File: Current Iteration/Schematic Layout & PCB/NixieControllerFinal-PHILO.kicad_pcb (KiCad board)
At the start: 2 copper layers, 47.3 x 96.8 mm, 100 parts, among them J1 Conn_01x10_Pin, J10 Conn_ARM_SWD_TagConnect_TC2030, J11 Conn_01x04_Socket, J12 Conn_01x03_Socket, J13 Conn_01x03_Socket, J16 Conn_01x08_Socket, J2 JST_EH_B4B, J3 Conn_01x10_Pin, J4 Conn_01x10_Pin, J5 Conn_01x10_Pin, J6 Conn_01x02, J7 Micro_SD_Card_Det1, J9 NixieIN, U1 HV5622PG, U10 NID1100, U11 TPS61040DBV, U13 STM32G0B1KEU6, U14 CM1224-04MR, U2 HV5622PG, U3 4504, U4 CM1224-04MR, U5 NCH6100HV, U6 CAP1206-x-SL, U7 NID1100, U8 MCP1700x-330xxTT, U9 MAX98357A

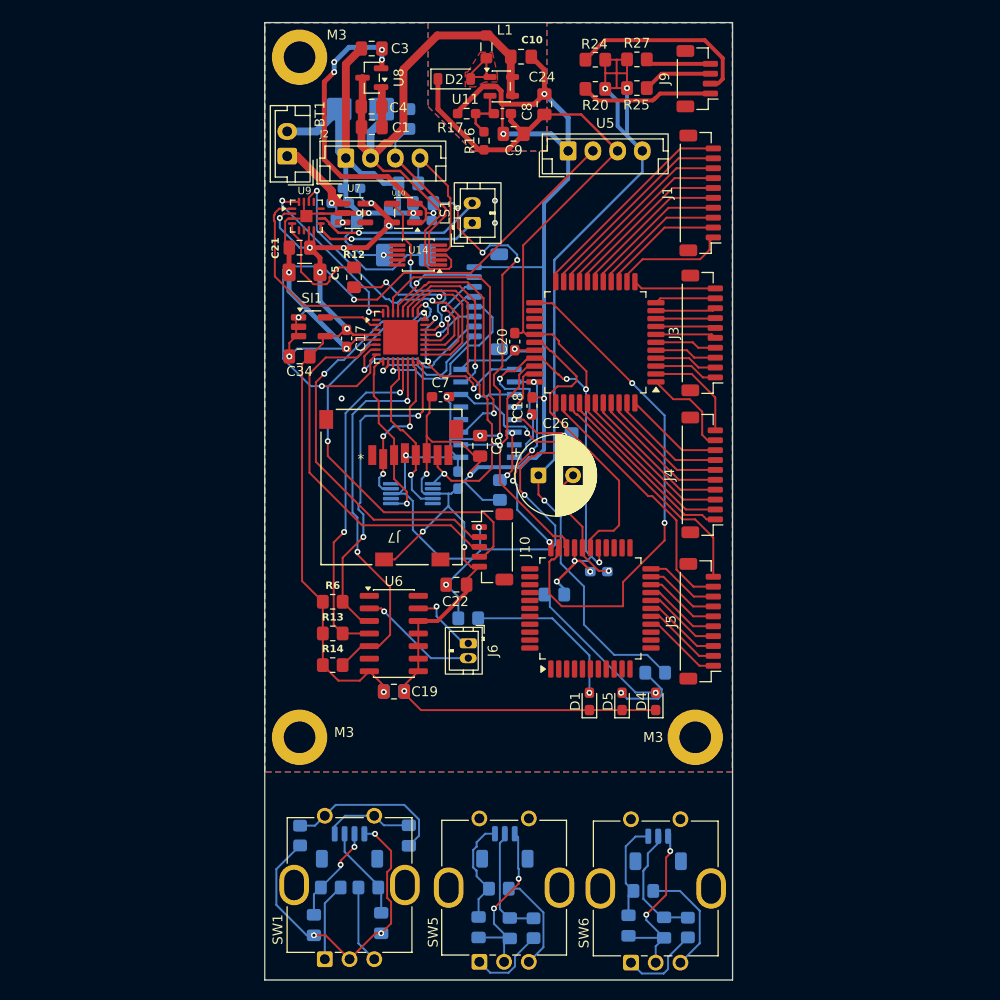
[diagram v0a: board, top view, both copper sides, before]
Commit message: Updated Readme with improved  firmware documentation/updated src code
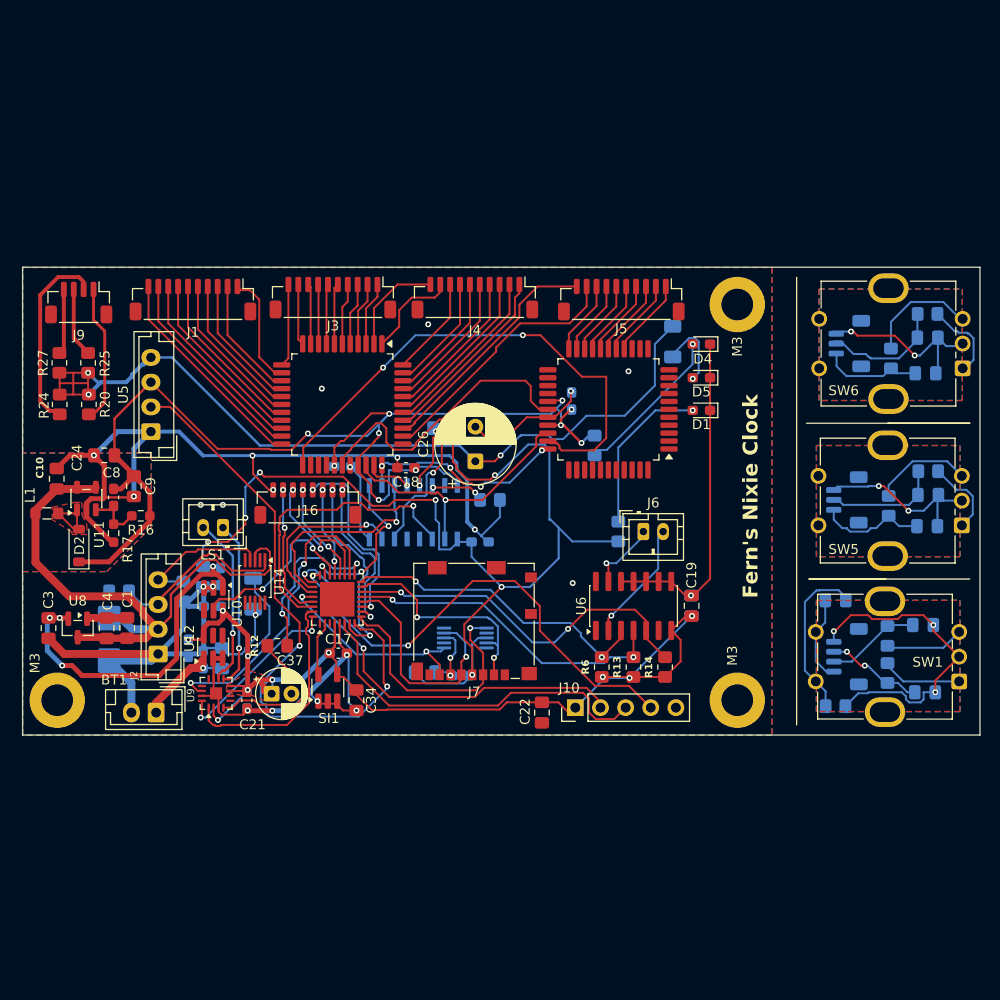
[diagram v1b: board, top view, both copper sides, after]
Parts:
- removed C5: 220uF, Capacitor_SMD:C_1206_3216Metric_Pad1.33x1.80mm_HandSolder
- removed U7: NID1100, Package_TO_SOT_SMD:SC-74A-5_1.55x2.9mm_P0.95mm
- added C30: 10uF 10V, Capacitor_SMD:C_0603_1608Metric_Pad1.08x0.95mm_HandSolder, B.Cu at (165.2, 106.7)
- added C37: 220uF Electrolytic, Capacitor_THT:CP_Radial_D5.0mm_P2.00mm, F.Cu at (167.7, 106.1)
- added U12: NID5100, Package_TO_SOT_SMD:SC-74-6_1.55x2.9mm_P0.95mm, F.Cu at (161.8, 101.4)
- C20, C6, C7: moved to B.Cu
- C21: footprint Capacitor_SMD:C_0805_2012Metric_Pad1.18x1.45mm_HandSolder -> Capacitor_SMD:C_0603_1608Metric_Pad1.08x0.95mm_HandSolder
- C29: footprint Capacitor_SMD:C_1808_4520Metric_Pad1.72x2.30mm_HandSolder -> Capacitor_SMD:C_1206_3216Metric_Pad1.33x1.80mm_HandSolder
- D1: value 3.3V+ -> 150060AS75000
- D4: value 12V+ -> 150060AS75000
- D5: value 170V+ -> 150060AS75000
- J10: footprint Connector_JST:JST_SH_BM05B-SRSS-TB_1x05-1MP_P1.00mm_Vertical -> Connector_PinHeader_2.54mm:PinHeader_1x05_P2.54mm_Vertical
- J16: moved to F.Cu
- J6: footprint Connector_JST:JST_ZH_B2B-ZR_1x02_P1.50mm_Vertical -> Connector_JST:JST_PH_B2B-PH-K_1x02_P2.00mm_Vertical
- J7: footprint footprints:MEM2061-01-188-00-A_GCT -> Connector_Card:microSD_HC_Molex_104031-0811
- R15: value 670 20% -> 2400 20%
- R19: value 11200 20% -> 34k 10%; footprint Resistor_SMD:R_0805_2012Metric_Pad1.20x1.40mm_HandSolder -> Resistor_SMD:R_1206_3216Metric_Pad1.30x1.75mm_HandSolder
- R5: value 86 20% -> 660 20%
- U10: value NID1100 -> NID5100; footprint Package_TO_SOT_SMD:SC-74A-5_1.55x2.9mm_P0.95mm -> Package_TO_SOT_SMD:SC-74-6_1.55x2.9mm_P0.95mm
- U14, U4: footprint Package_SO:MSOP-10_3x3mm_P0.5mm -> Package_SO:TSSOP-10_3x3mm_P0.5mm
- moved SW1 70.0 mm to (237.2, 104.8), turned to 180 degrees
- moved REF** 69.5 mm to (146.0, 106.8), turned to 90 degrees
- moved SW6 68.8 mm to (237.5, 73.2), turned to 180 degrees
- moved C3 67.1 mm to (145.1, 99.5), turned to -90 degrees
- moved R26 66.6 mm to (234.0, 67.7), turned to 180 degrees
- moved J9 66.5 mm to (148.2, 66.5), turned to 180 degrees
- moved C16 66.1 mm to (233.7, 106.0), turned to 0 degrees
- moved R27 66.0 mm to (146.2, 72.7), turned to 90 degrees
- moved SW5 65.8 mm to (237.4, 89.1), turned to 180 degrees
- moved C14 65.3 mm to (234.0, 70.1), turned to 0 degrees
- moved L1 64.8 mm to (144.9, 87.9), turned to 0 degrees
- moved R24 64.4 mm to (146.2, 76.8), turned to -90 degrees
- moved C10 63.4 mm to (145.9, 84.4), turned to 90 degrees
- moved C13 63.4 mm to (233.8, 73.7), turned to 0 degrees
- moved U8 63.1 mm to (148.1, 99.5), turned to -90 degrees
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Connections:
- net /ROT1C renamed /ROT_3A
- net /ROT2C renamed /ROT_3B
- C13 pad 1: /ROT2B -> /ROT_1B
- C14 pad 1: /ROT1B -> /ROT_1A
- C15 pad 1: /ROT2A -> /ROT_2B
- C16 pad 1: /ROT1A -> /ROT_2A
- C22 pad 1: +3.3V -> +V_CRIT
- J10 pad 1: +3.3V -> +V_CRIT
- J11 pad 2: /ROT2A -> /ROT_2B
- J11 pad 3: /ROT1A -> /ROT_2A
- J12 pad 1: /ROT2B -> /ROT_1B
- J12 pad 2: /ROT1B -> /ROT_1A
- R18 pad 1: /ROT2A -> /ROT_2B
- R23 pad 1: /ROT2B -> /ROT_1B
- R26 pad 2: /ROT1B -> /ROT_1A
- R29 pad 2: /ROT1A -> /ROT_2A
- U10 pad 3: +3.3V -> GND
- U10 pad 4: Net-(U10-ST) -> unconnected-(U10-NC-Pad4)
- U10 pad 5: +V_CRIT -> Net-(U10-ST)
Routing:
- net GND: track 296.7 -> 246.3 mm, vias 22 -> 25
- net /SD_MISO: track 37.4 -> 21.5 mm, vias 1 -> 2
- net +V_CRIT: track 94.4 -> 108.2 mm, vias 8 -> 10
- net /ROT_1A: track 0.00 -> 12.3 mm
- net /ROT_1B: track 0.00 -> 10.1 mm
- net /ROT_2A: track 0.00 -> 9.89 mm, vias 0 -> 2
- net /ROT1B: track 23.3 -> 13.5 mm, vias 1 -> 2
- net /ROT_2B: track 0.00 -> 8.90 mm
- net +3.3V: track 137.5 -> 146.3 mm, vias 16 -> 12
- net /ROT2B: track 27.8 -> 19.3 mm, vias 1 -> 2
- net /SD_MOSI: track 18.0 -> 25.9 mm
- net /ROT2A: track 17.5 -> 10.3 mm, vias 1 -> 2
- net /SD_NSS: track 16.5 -> 22.9 mm, vias 3 -> 2
- net /ROT1A: track 20.0 -> 13.7 mm, vias 3 -> 2
- net /SD_SCK: track 17.3 -> 23.4 mm
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- added copper zone on F.Cu, net +V_CRIT
- added copper zone on B.Cu, net /GNDA
- added copper zone on F.Cu, net /GNDA
- added copper zone on B.Cu, net /GNDB
- added copper zone on F.Cu, net /GNDB
- added copper zone on B.Cu, net /GNDC
- added copper zone on F.Cu, net /GNDC
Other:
- board size 47.3 x 96.8 mm -> 96.8 x 47.3 mm
- board text added: "Fern's Nixie Clock"
